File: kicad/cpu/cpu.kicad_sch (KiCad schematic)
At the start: 10 parts, among them J1 Board Connector, J8 Conn_02x04_Counter_Clockwise, U1 W65C02SxP

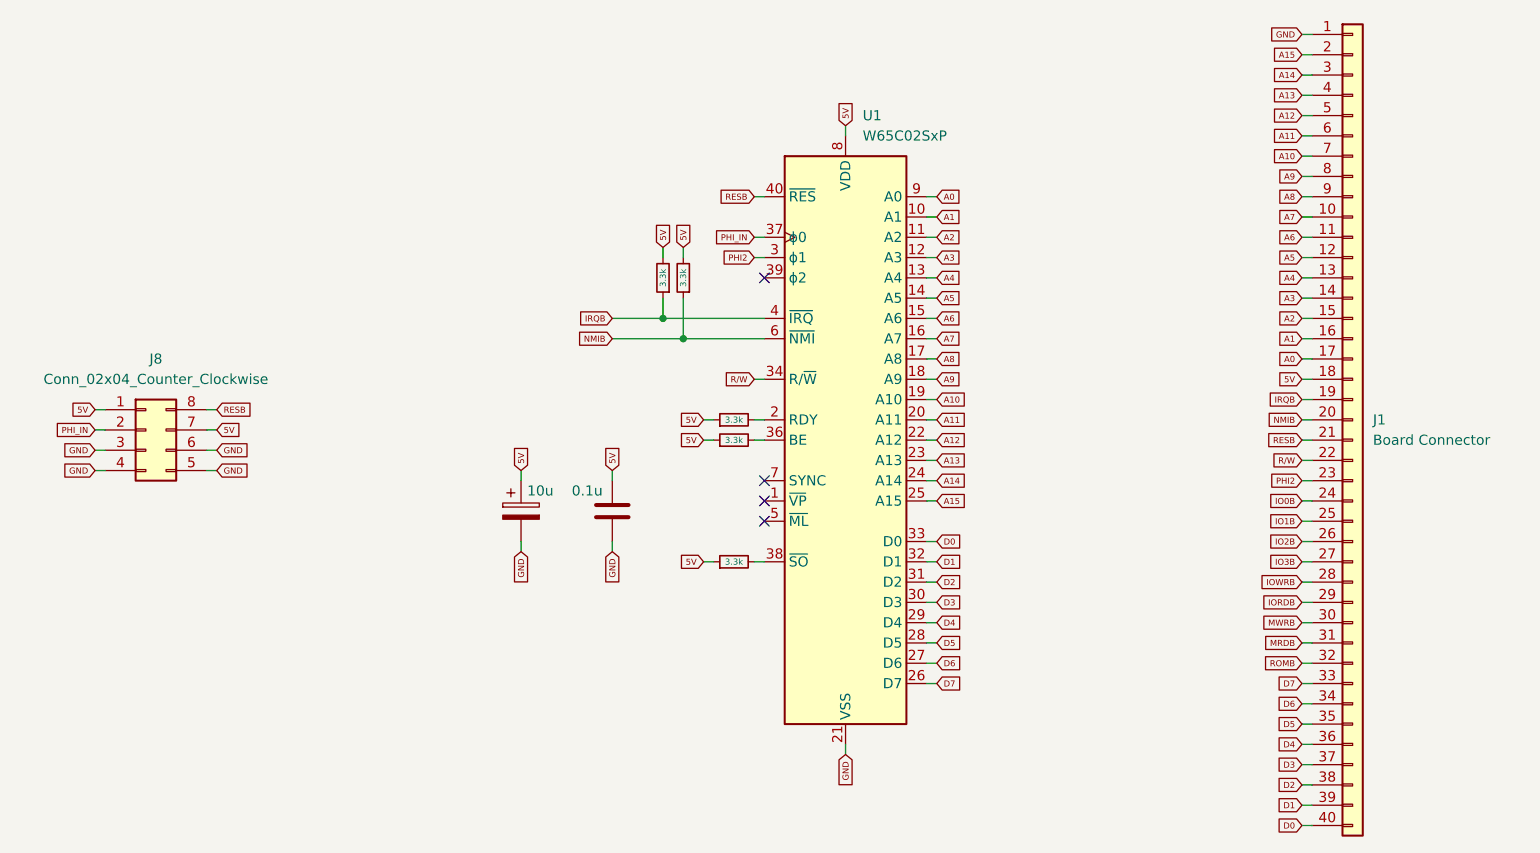
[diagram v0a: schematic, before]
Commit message: integrated wozmon, updated kicad to specify phi1o
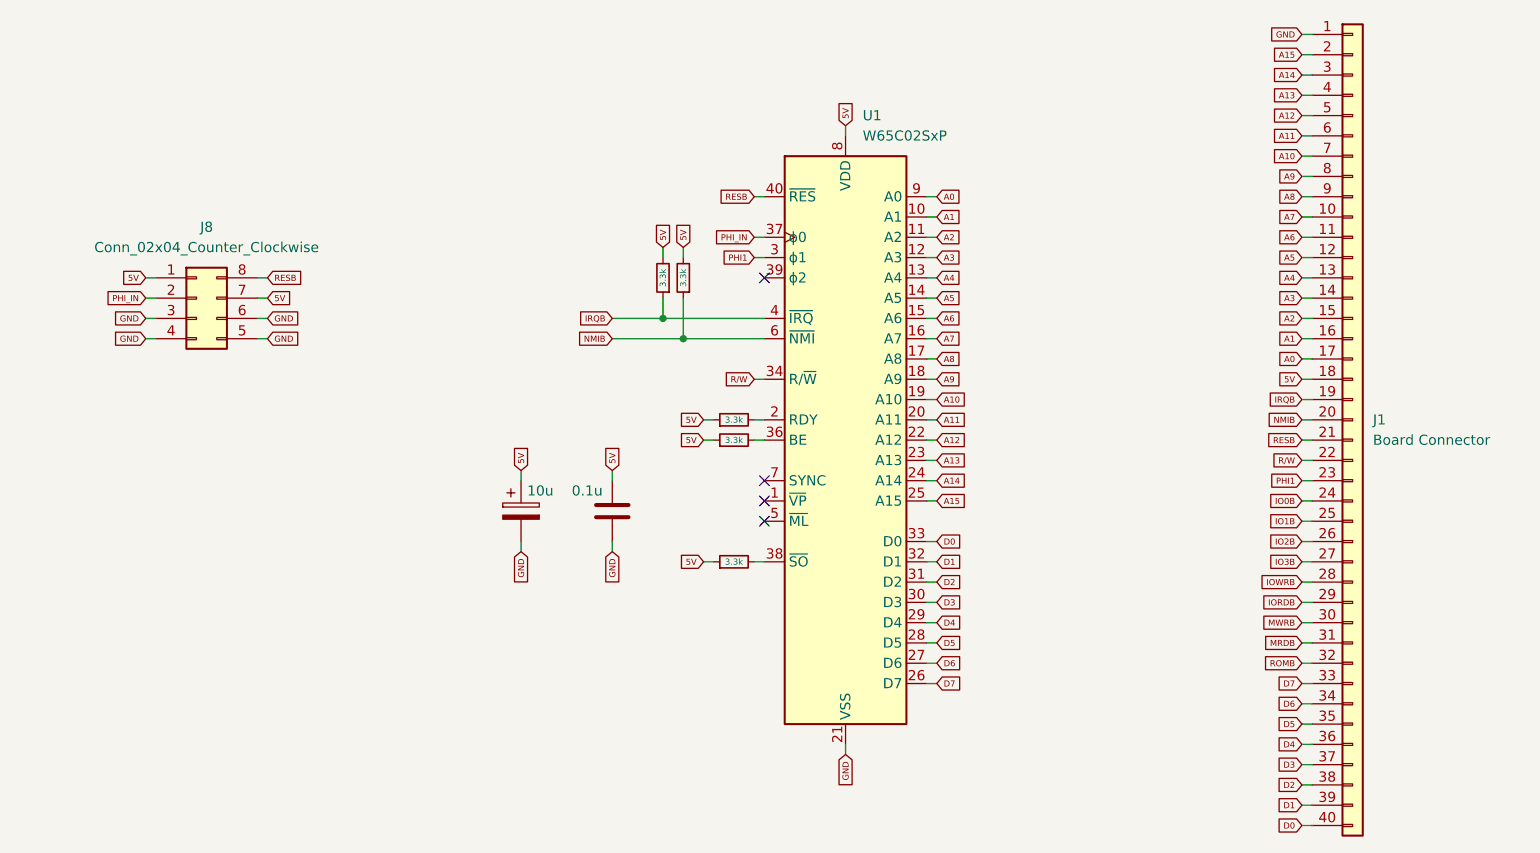
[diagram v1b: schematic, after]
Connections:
- net PHI2 renamed PHI1
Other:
- moved on the sheet: J8
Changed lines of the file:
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@@
 	(wire
 		(pts
-			(xy 91.44 92.71) (xy 92.71 92.71)
+			(xy 97.79 76.2) (xy 99.06 76.2)
 		)
 		(stroke
@@
 	(wire
 		(pts
-			(xy 91.44 100.33) (xy 92.71 100.33)
+			(xy 97.79 83.82) (xy 99.06 83.82)
 		)
 		(stroke
@@
 	(wire
 		(pts
-			(xy 105.41 97.79) (xy 106.68 97.79)
+			(xy 111.76 81.28) (xy 113.03 81.28)
 		)
 		(stroke
@@
 	(wire
 		(pts
-			(xy 91.44 97.79) (xy 92.71 97.79)
+			(xy 97.79 81.28) (xy 99.06 81.28)
 		)
 		(stroke
@@
 	(wire
 		(pts
-			(xy 105.41 95.25) (xy 106.68 95.25)
+			(xy 111.76 78.74) (xy 113.03 78.74)
 		)
 		(stroke
@@
 	(wire
 		(pts
-			(xy 105.41 100.33) (xy 106.68 100.33)
+			(xy 111.76 83.82) (xy 113.03 83.82)
 		)
 		(stroke
@@
 	(wire
 		(pts
-			(xy 91.44 95.25) (xy 92.71 95.25)
+			(xy 97.79 78.74) (xy 99.06 78.74)
 		)
 		(stroke
@@
 	(wire
 		(pts
-			(xy 105.41 92.71) (xy 106.68 92.71)
+			(xy 111.76 76.2) (xy 113.03 76.2)
 		)
 		(stroke
@@
 	(global_label "GND"
 		(shape input)
-		(at 106.68 100.33 0)
-		(fields_autoplaced yes)
-		(effects
-			(font
-				(size 0.762 0.762)
-			)
-			(justify left)
-		)
-		(property "Intersheetrefs" "${INTERSHEET_REFS}"
-			(at 110.7937 100.33 0)
+		(at 113.03 83.82 0)
+		(fields_autoplaced yes)
+		(effects
+			(font
+				(size 0.762 0.762)
+			)
+			(justify left)
+		)
+		(property "Intersheetrefs" "${INTERSHEET_REFS}"
+			(at 117.1437 83.82 0)
 			(hide yes)
 			(show_name no)
@@
 	(global_label "GND"
 		(shape input)
-		(at 106.68 97.79 0)
-		(fields_autoplaced yes)
-		(effects
-			(font
-				(size 0.762 0.762)
-			)
-			(justify left)
-		)
-		(property "Intersheetrefs" "${INTERSHEET_REFS}"
-			(at 110.7937 97.79 0)
+		(at 113.03 81.28 0)
+		(fields_autoplaced yes)
+		(effects
+			(font
+				(size 0.762 0.762)
+			)
+			(justify left)
+		)
+		(property "Intersheetrefs" "${INTERSHEET_REFS}"
+			(at 117.1437 81.28 0)
 			(hide yes)
 			(show_name no)
@@
 		)
 	)
-	(global_label "PHI2"
+	(global_label "PHI1"
 		(shape input)
 		(at 242.57 101.6 180)
@@
 	(global_label "GND"
 		(shape input)
-		(at 91.44 100.33 180)
-		(fields_autoplaced yes)
-		(effects
-			(font
-				(size 0.762 0.762)
-			)
-			(justify right)
-		)
-		(property "Intersheetrefs" "${INTERSHEET_REFS}"
-			(at 87.3263 100.33 0)
+		(at 97.79 83.82 180)
+		(fields_autoplaced yes)
+		(effects
+			(font
+				(size 0.762 0.762)
+			)
+			(justify right)
+		)
+		(property "Intersheetrefs" "${INTERSHEET_REFS}"
+			(at 93.6763 83.82 0)
 			(hide yes)
 			(show_name no)
@@
 	(global_label "RESB"
 		(shape input)
-		(at 106.68 92.71 0)
-		(fields_autoplaced yes)
-		(effects
-			(font
-				(size 0.762 0.762)
-			)
-			(justify left)
-		)
-		(property "Intersheetrefs" "${INTERSHEET_REFS}"
-			(at 111.4105 92.71 0)
+		(at 113.03 76.2 0)
+		(fields_autoplaced yes)
+		(effects
+			(font
+				(size 0.762 0.762)
+			)
+			(justify left)
+		)
+		(property "Intersheetrefs" "${INTERSHEET_REFS}"
+			(at 117.7605 76.2 0)
 			(hide yes)
 			(show_name no)
@@
 	(global_label "5V"
 		(shape input)
-		(at 91.44 92.71 180)
-		(fields_autoplaced yes)
-		(effects
-			(font
-				(size 0.762 0.762)
-			)
-			(justify right)
-		)
-		(property "Intersheetrefs" "${INTERSHEET_REFS}"
-			(at 88.2698 92.71 0)
+		(at 97.79 76.2 180)
+		(fields_autoplaced yes)
+		(effects
+			(font
+				(size 0.762 0.762)
+			)
+			(justify right)
+		)
+		(property "Intersheetrefs" "${INTERSHEET_REFS}"
+			(at 94.6198 76.2 0)
 			(hide yes)
 			(show_name no)
@@
 	(global_label "GND"
 		(shape input)
-		(at 91.44 97.79 180)
-		(fields_autoplaced yes)
-		(effects
-			(font
-				(size 0.762 0.762)
-			)
-			(justify right)
-		)
-		(property "Intersheetrefs" "${INTERSHEET_REFS}"
-			(at 87.3263 97.79 0)
-			(hide yes)
-			(show_name no)
-			(do_not_autoplace no)
-			(effects
-				(font
-					(size 1.27 1.27)
-				)
-				(justify right)
-			)
-		)
-	)
-	(global_label "PHI2"
+		(at 97.79 81.28 180)
+		(fields_autoplaced yes)
+		(effects
+			(font
+				(size 0.762 0.762)
+			)
+			(justify right)
+		)
+		(property "Intersheetrefs" "${INTERSHEET_REFS}"
+			(at 93.6763 81.28 0)
+			(hide yes)
+			(show_name no)
+			(do_not_autoplace no)
+			(effects
+				(font
+					(size 1.27 1.27)
+				)
+				(justify right)
+			)
+		)
+	)
+	(global_label "PHI1"
 		(shape input)
 		(at 173.99 73.66 180)
@@
 	(global_label "5V"
 		(shape input)
-		(at 106.68 95.25 0)
-		(fields_autoplaced yes)
-		(effects
-			(font
-				(size 0.762 0.762)
-			)
-			(justify left)
-		)
-		(property "Intersheetrefs" "${INTERSHEET_REFS}"
-			(at 109.8502 95.25 0)
+		(at 113.03 78.74 0)
+		(fields_autoplaced yes)
+		(effects
+			(font
+				(size 0.762 0.762)
+			)
+			(justify left)
+		)
+		(property "Intersheetrefs" "${INTERSHEET_REFS}"
+			(at 116.2002 78.74 0)
 			(hide yes)
 			(show_name no)
@@
 	(global_label "PHI_IN"
 		(shape input)
-		(at 91.44 95.25 180)
-		(fields_autoplaced yes)
-		(effects
-			(font
-				(size 0.762 0.762)
-			)
-			(justify right)
-		)
-		(property "Intersheetrefs" "${INTERSHEET_REFS}"
-			(at 85.9836 95.25 0)
+		(at 97.79 78.74 180)
+		(fields_autoplaced yes)
+		(effects
+			(font
+				(size 0.762 0.762)
+			)
+			(justify right)
+		)
+		(property "Intersheetrefs" "${INTERSHEET_REFS}"
+			(at 92.3336 78.74 0)
 			(hide yes)
 			(show_name no)
@@
 	(symbol
 		(lib_id "Connector_Generic:Conn_02x04_Counter_Clockwise")
-		(at 97.79 95.25 0)
+		(at 104.14 78.74 0)
 		(unit 1)
 		(body_style 1)
@@
 		(fields_autoplaced yes)
 		(property "Reference" "J8"
-			(at 99.06 86.36 0)
+			(at 105.41 69.85 0)
 			(show_name no)
 			(do_not_autoplace no)
@@
 		)
 		(property "Value" "Conn_02x04_Counter_Clockwise"
-			(at 99.06 88.9 0)
+			(at 105.41 72.39 0)
 			(show_name no)
 			(do_not_autoplace no)
@@
 		)
 		(property "Footprint" "Connector_PinHeader_2.54mm:PinHeader_2x04_P2.54mm_Horizontal"
-			(at 97.79 95.25 0)
+			(at 104.14 78.74 0)
 			(hide yes)
 			(show_name no)
@@
 		)
 		(property "Datasheet" ""
-			(at 97.79 95.25 0)
+			(at 104.14 78.74 0)
 			(hide yes)
 			(show_name no)
@@
 		)
 		(property "Description" "Generic connector, double row, 02x04, counter clockwise pin numbering scheme (similar to DIP package numbering), script generated (kicad-library-utils/schlib/autogen/connector/)"
-			(at 97.79 95.25 0)
-			(hide yes)
-			(show_name no)
+			(at 104.14 78.74 0)
+			(hide yes)
+			(show_name no)
